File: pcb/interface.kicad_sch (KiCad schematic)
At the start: 21 parts

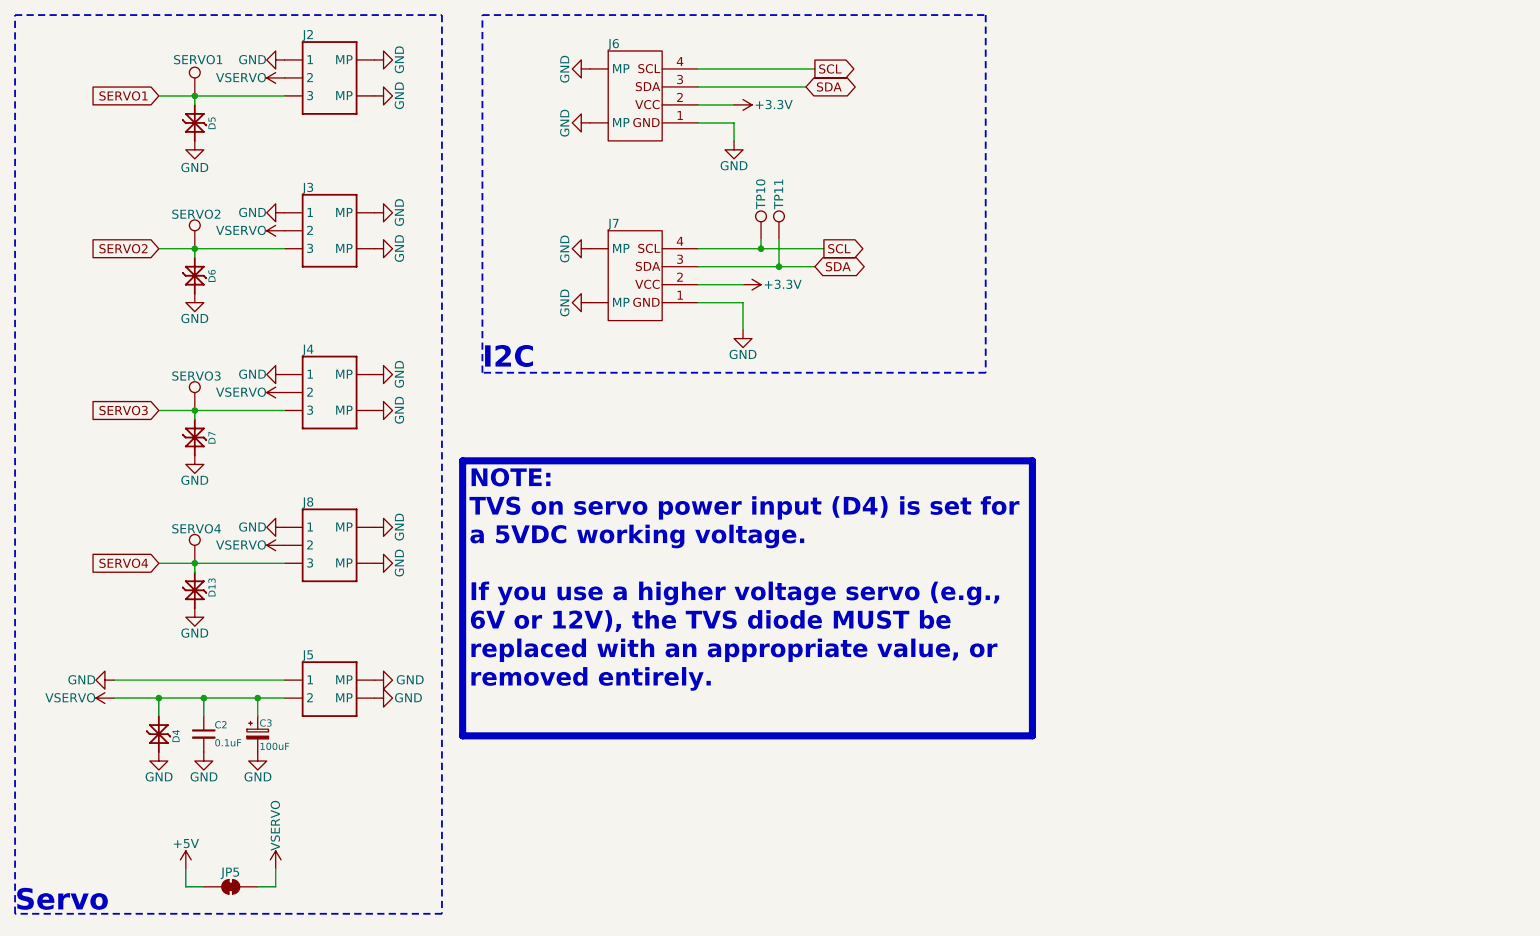
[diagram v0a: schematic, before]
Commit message: Redesign with SMT32
Complete redesign using SMT32 instead of ATTINY.
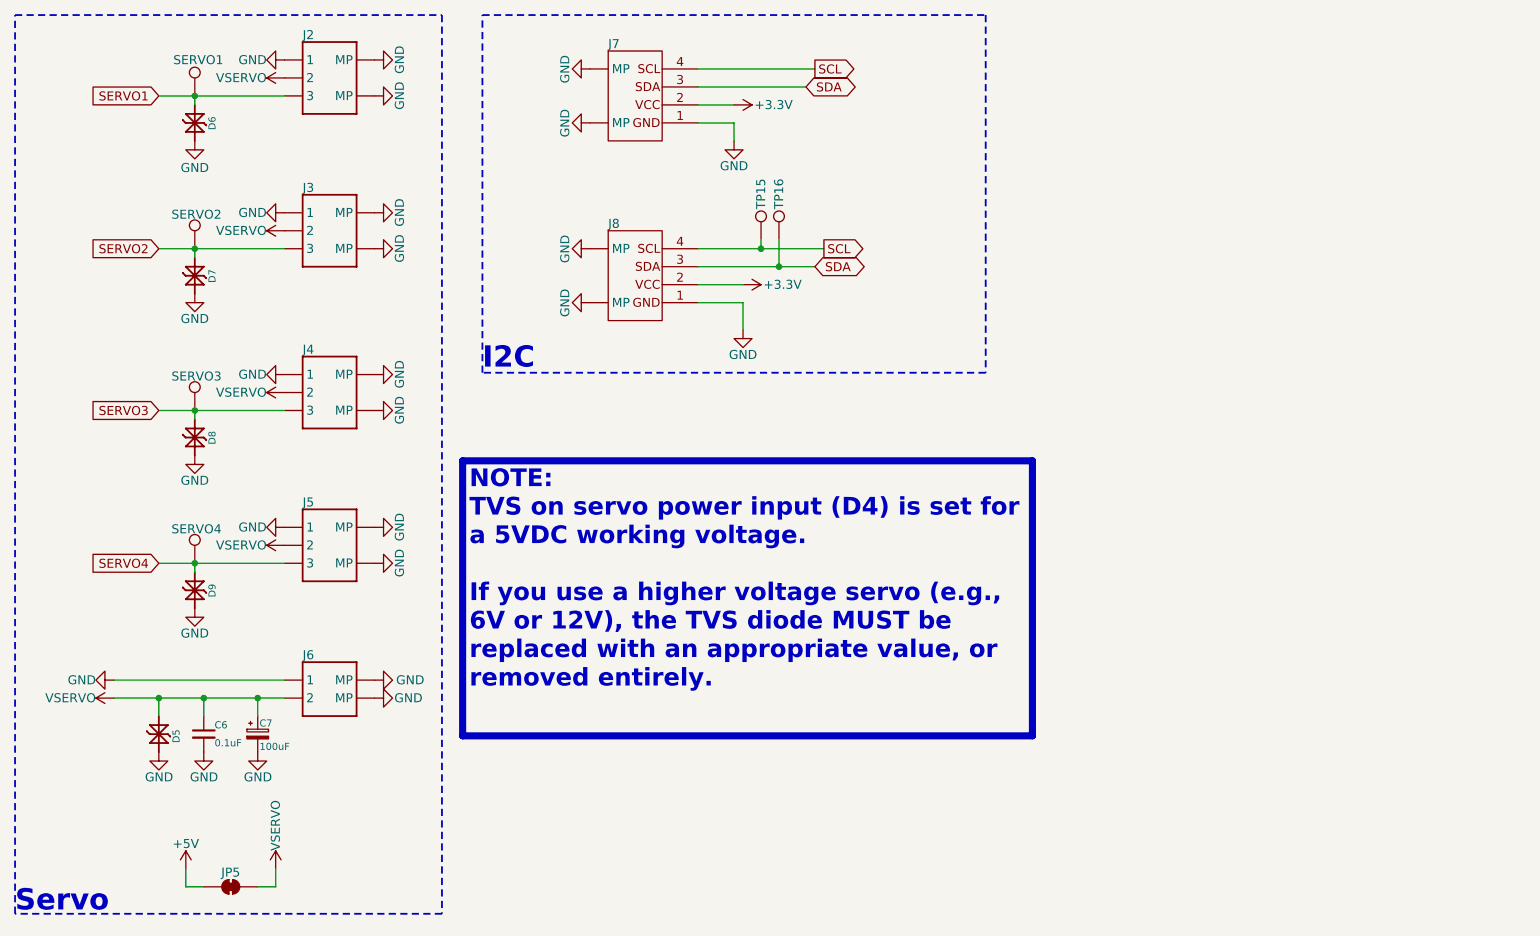
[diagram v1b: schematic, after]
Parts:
- renumbered C2 to C6, C3 to C7, D4 to D5, D5 to D6, D6 to D7, D7 to D8, D13 to D9, J8 to J5, J5 to J6, J6 to J7, J7 to J8, TP7 to TP11, TP8 to TP12, TP9 to TP13, TP12 to TP14, TP10 to TP15, TP11 to TP16

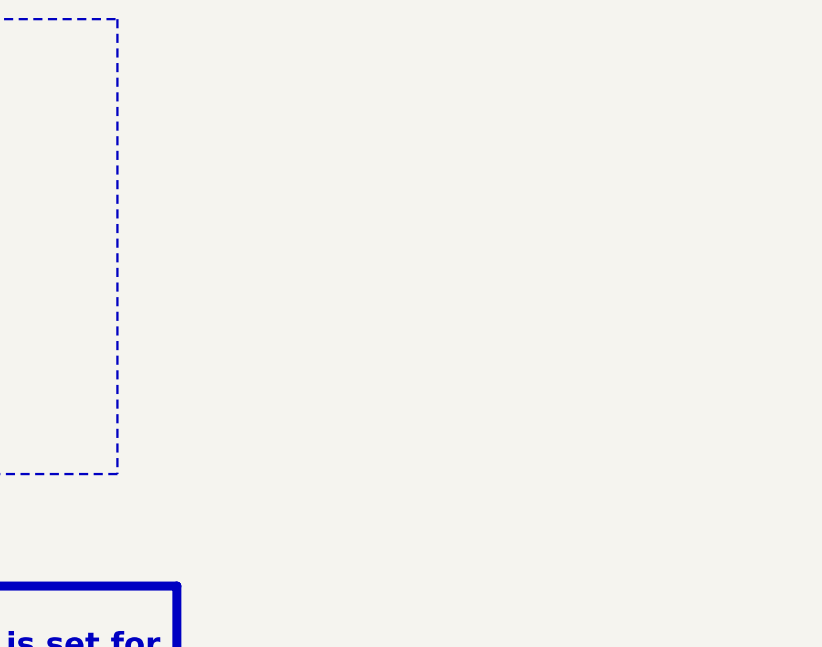
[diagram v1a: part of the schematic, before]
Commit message: Rearranged parts
Moved cap and power connector for SV power.
Moved SV PWR LED.
Moved reset switch.
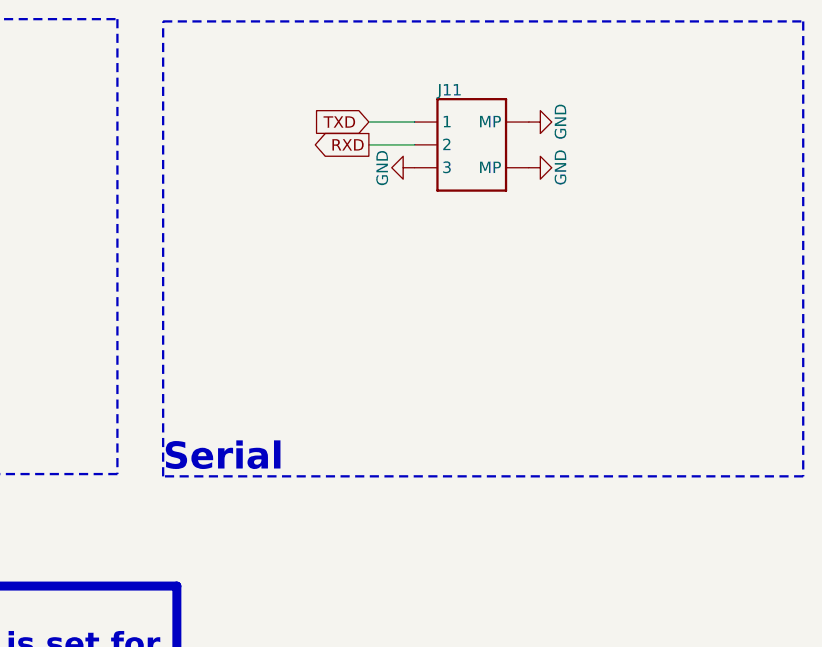
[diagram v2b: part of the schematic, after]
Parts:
- added J11: ~, CRGM Connector:JST_SH_BM03B-SRSS-TB_1x03-1MP_P1.00mm_Vertical, symbol CRGM Connector:JST-SH-3
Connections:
- net GND: now also J11.0 (MP), J11.3, J11.4 (MP)
- new net RXD: J11.2
- new net TXD: J11.1
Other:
- note added: "Serial"

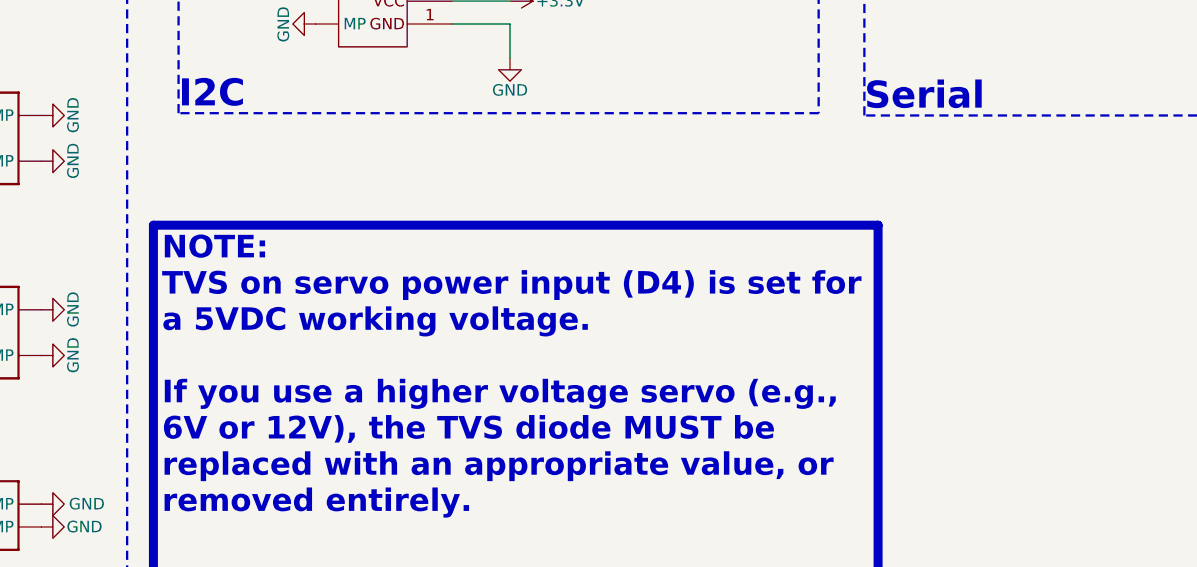
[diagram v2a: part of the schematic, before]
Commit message: Fixed models; adjusted layout
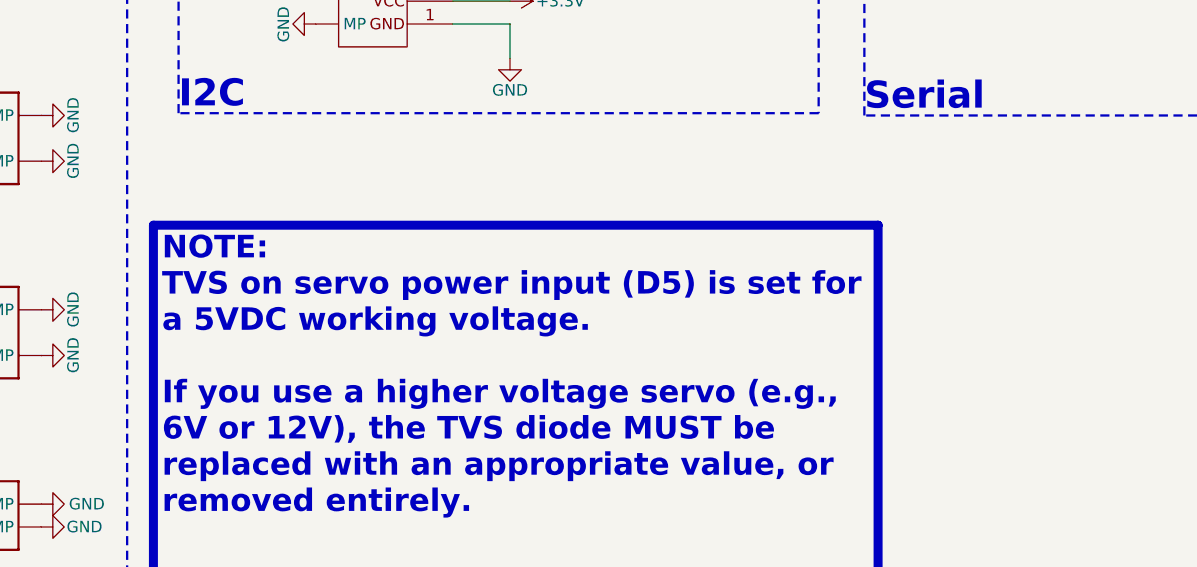
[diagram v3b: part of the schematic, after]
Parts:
- J7, J8: LCSC C2919601 -> C2904986
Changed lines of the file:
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@@
 		)
 	)
-	(text_box "NOTE:\nTVS on servo power input (D4) is set for a 5VDC working voltage.\n\nIf you use a higher voltage servo (e.g., 6V or 12V), the TVS diode MUST be replaced with an appropriate value, or removed entirely."
+	(text_box "NOTE:\nTVS on servo power input (D5) is set for a 5VDC working voltage.\n\nIf you use a higher voltage servo (e.g., 6V or 12V), the TVS diode MUST be replaced with an appropriate value, or removed entirely."
 		(exclude_from_sim no)
 		(at 88.646 88.392 0)
@@
 			)
 		)
-		(property "LCSC" "C2919601"
+		(property "LCSC" "C2904986"
 			(at 114.046 56.642 0)
 			(effects
@@
 			)
 		)
-		(property "LCSC" "C2919601"
+		(property "LCSC" "C2904986"
 			(at 114.046 82.042 0)
 			(effects

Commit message: Fixed massive part/bom mismatches.
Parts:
- J11, J2, J3, J4, J5: Digikey 455-BM04B-SRSS-TBTR-ND -> 455-BM03B-SRSS-TBTR-ND; LCSC C2919601 -> C2904985; MPN BM04B-SRSS-TB -> BM03B-SRSS-TB; Mouser 306-BM04BSRSSTBTLFSN -> 306-BM03BSRSSTBTLFSN
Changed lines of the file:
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@@
 			)
 		)
-		(property "MPN" "BM04B-SRSS-TB"
+		(property "MPN" "BM03B-SRSS-TB"
 			(at 66.04 67.818 0)
 			(effects
@@
 			)
 		)
-		(property "Digikey" "455-BM04B-SRSS-TBTR-ND"
+		(property "Digikey" "455-BM03B-SRSS-TBTR-ND"
 			(at 66.04 72.136 0)
 			(effects
@@
 			)
 		)
-		(property "Mouser" "306-BM04BSRSSTBTLFSN"
+		(property "Mouser" "306-BM03BSRSSTBTLFSN"
 			(at 66.04 74.676 0)
 			(effects
@@
 			)
 		)
-		(property "LCSC" "C2919601"
+		(property "LCSC" "C2904985"
 			(at 66.04 69.85 0)
 			(effects
@@
 			)
 		)
-		(property "MPN" "BM04B-SRSS-TB"
+		(property "MPN" "BM03B-SRSS-TB"
 			(at 66.04 112.268 0)
 			(effects
@@
 			)
 		)
-		(property "Digikey" "455-BM04B-SRSS-TBTR-ND"
+		(property "Digikey" "455-BM03B-SRSS-TBTR-ND"
 			(at 66.04 116.586 0)
 			(effects
@@
 			)
 		)
-		(property "Mouser" "306-BM04BSRSSTBTLFSN"
+		(property "Mouser" "306-BM03BSRSSTBTLFSN"
 			(at 66.04 119.126 0)
 			(effects
@@
 			)
 		)
-		(property "LCSC" "C2919601"
+		(property "LCSC" "C2904985"
 			(at 66.04 114.3 0)
 			(effects
@@
 			)
 		)
-		(property "MPN" "BM04B-SRSS-TB"
+		(property "MPN" "BM03B-SRSS-TB"
 			(at 66.04 90.678 0)
 			(effects
@@
 			)
 		)
-		(property "Digikey" "455-BM04B-SRSS-TBTR-ND"
+		(property "Digikey" "455-BM03B-SRSS-TBTR-ND"
 			(at 66.04 94.996 0)
 			(effects
@@
 			)
 		)
-		(property "Mouser" "306-BM04BSRSSTBTLFSN"
+		(property "Mouser" "306-BM03BSRSSTBTLFSN"
 			(at 66.04 97.536 0)
 			(effects
@@
 			)
 		)
-		(property "LCSC" "C2919601"
+		(property "LCSC" "C2904985"
 			(at 66.04 92.71 0)
 			(effects
@@
 			)
 		)
-		(property "MPN" "BM04B-SRSS-TB"
+		(property "MPN" "BM03B-SRSS-TB"
 			(at 66.04 46.228 0)
 			(effects
@@
 			)
 		)
-		(property "Digikey" "455-BM04B-SRSS-TBTR-ND"
+		(property "Digikey" "455-BM03B-SRSS-TBTR-ND"
 			(at 66.04 50.546 0)
 			(effects
@@
 			)
 		)
-		(property "Mouser" "306-BM04BSRSSTBTLFSN"
+		(property "Mouser" "306-BM03BSRSSTBTLFSN"
 			(at 66.04 53.086 0)
 			(effects
@@
 			)
 		)
-		(property "LCSC" "C2919601"
+		(property "LCSC" "C2904985"
 			(at 66.04 48.26 0)
 			(effects
@@
 			)
 		)
-		(property "MPN" "BM04B-SRSS-TB"
+		(property "MPN" "BM03B-SRSS-TB"
 			(at 198.12 51.308 0)
 			(effects
@@
 			)
 		)
-		(property "Digikey" "455-BM04B-SRSS-TBTR-ND"
+		(property "Digikey" "455-BM03B-SRSS-TBTR-ND"
 			(at 198.12 55.626 0)
 			(effects
@@
 			)
 		)
-		(property "Mouser" "306-BM04BSRSSTBTLFSN"
+		(property "Mouser" "306-BM03BSRSSTBTLFSN"
 			(at 198.12 58.166 0)
 			(effects
@@
 			)
 		)
-		(property "LCSC" "C2919601"
+		(property "LCSC" "C2904985"
 			(at 198.12 53.34 0)
 			(effects
